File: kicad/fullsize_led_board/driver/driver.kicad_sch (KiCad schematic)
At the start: 131 parts, among them J4 Anodes Header, J5 Cathodes Header, Q1 SQ2351CES, Q10 SQ2351CES, Q11 SQ2351CES, Q12 SQ2351CES, Q13 SQ2351CES, Q14 SQ2351CES, Q15 SQ2351CES, Q16 SQ2351CES, Q17 SQ2351CES, Q18 SQ2351CES, Q19 SQ2351CES, Q2 SQ2351CES, Q20 SQ2351CES, Q21 SQ2351CES, Q22 SQ2351CES, Q23 SQ2351CES, Q24 SQ2351CES, Q3 SQ2351CES, Q4 SQ2351CES, Q5 SQ2351CES, Q6 SQ2351CES, Q7 SQ2351CES, Q8 SQ2351CES, Q9 SQ2351CES, U1 74HCT541, U2 74HCT595, U3 74HCT595, U4 74HCT595, U5 TPIC6B595N, U6 TPIC6B595N, U7 TPIC6B595N, U8 TPIC6B595N

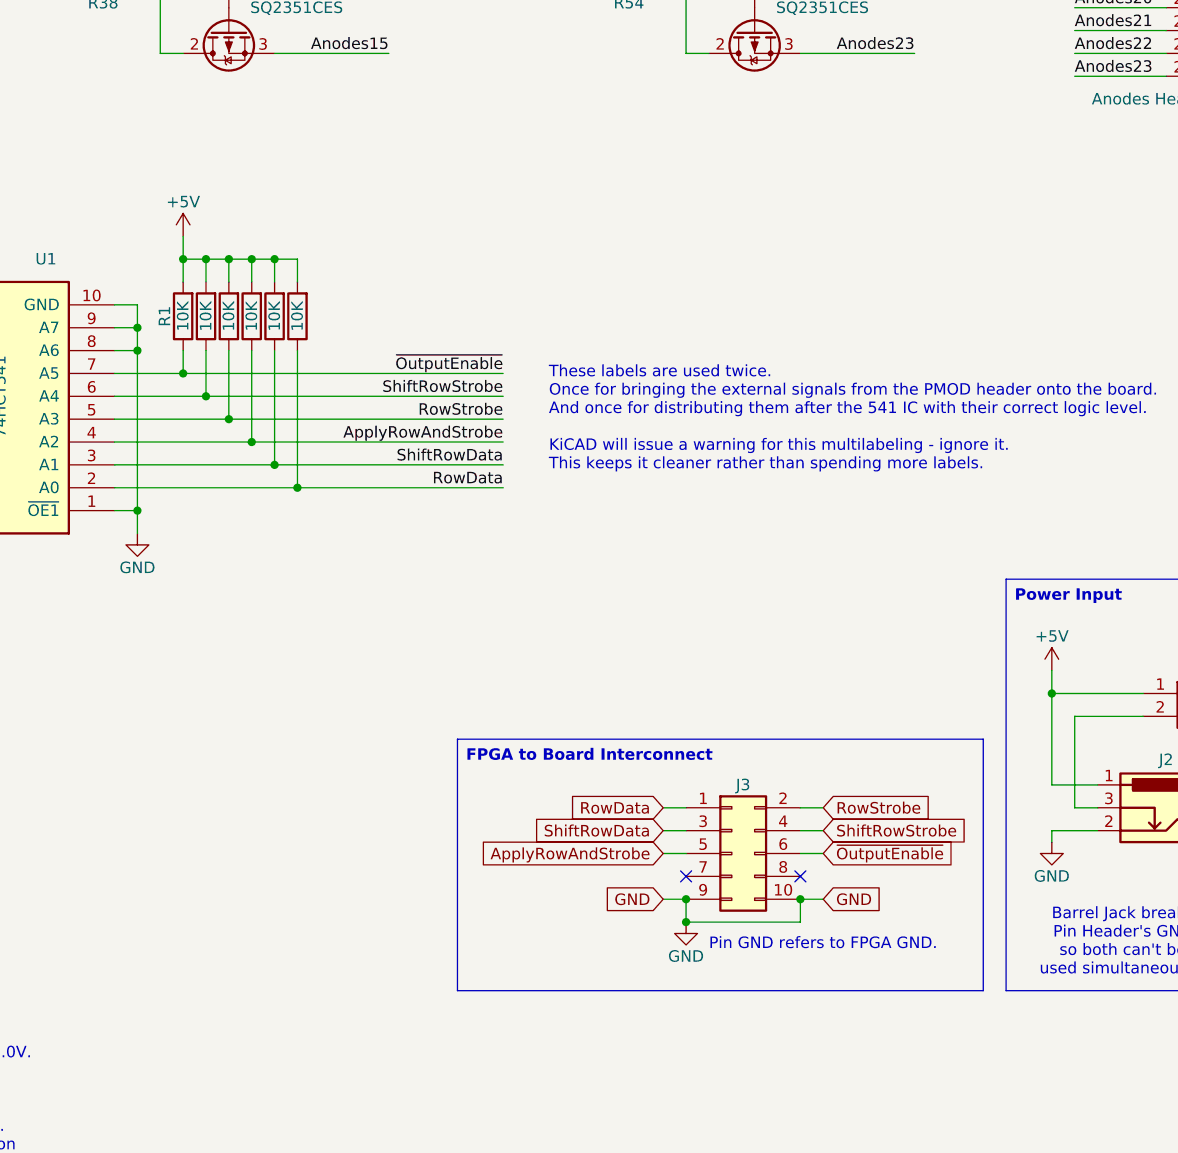
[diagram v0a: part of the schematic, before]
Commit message: fullsize led board: moved pullups to +3.3v of pmod
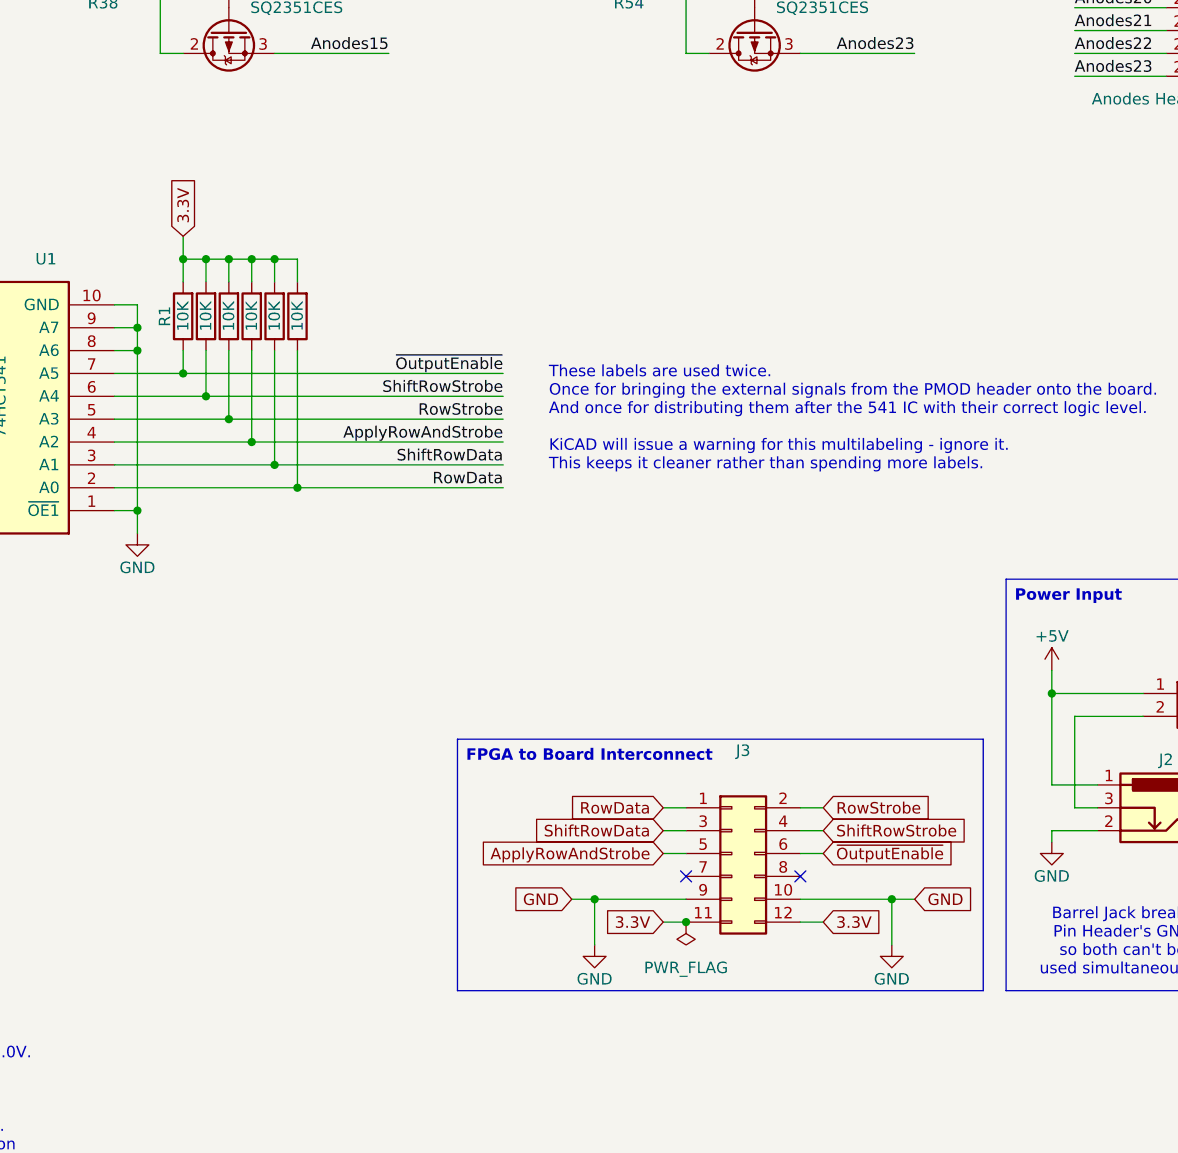
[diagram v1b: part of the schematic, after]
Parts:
- removed J3: ~, Connector_PinHeader_2.54mm:PinHeader_2x05_P2.54mm_Horizontal, symbol Connector_Generic:Conn_02x05_Odd_Even
- added J3: ~, Connector_PinHeader_2.54mm:PinHeader_2x06_P2.54mm_Horizontal, symbol Connector_Generic:Conn_02x06_Odd_Even
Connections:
- net +5V: no longer R1.2, R2.2, R3.2, R4.2, R5.2, R6.2
- net ApplyRowAndStrobe: now also J3.5 (Pin_5)
- net GND: now also J3.10 (Pin_10), J3.9 (Pin_9)
- net RowData: now also J3.1 (Pin_1)
- net RowStrobe: now also J3.2 (Pin_2)
- net ShiftRowData: now also J3.3 (Pin_3)
- net ShiftRowStrobe: now also J3.4 (Pin_4)
- net ~{OutputEnable}: now also J3.6 (Pin_6)
- new net 3.3V: J3.11 (Pin_11), J3.12 (Pin_12), R1.2, R2.2, R3.2, R4.2, R5.2, R6.2
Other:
- note removed: "Pin GND refers to FPGA GND."
